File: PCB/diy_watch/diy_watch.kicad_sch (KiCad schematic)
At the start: 39 parts, among them J1 USB_B_Micro, SW1 SW_Push, U1 W25Q32JVSS, U2 DS3231MZ, U3 RP2040, U5 LTC4054ES5-4.2, U7 XC6210B332MR, Y1 12MHz_crystal

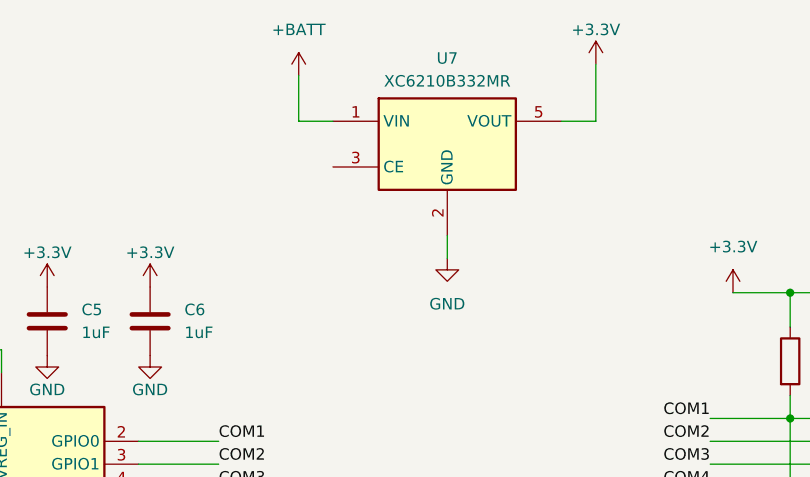
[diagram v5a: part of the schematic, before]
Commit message: Added caps to regulator, Changed edge cut
Adding missing pullup on switch
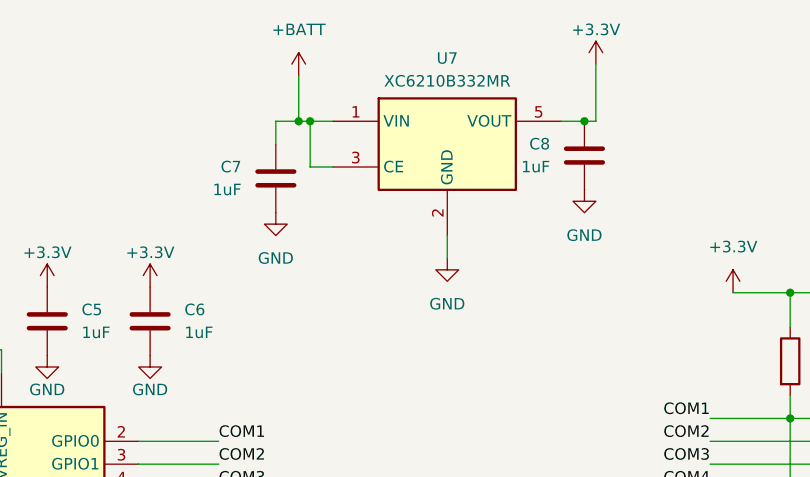
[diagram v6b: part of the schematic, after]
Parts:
- added C7, C8: 1uF, Capacitor_SMD:C_0402_1005Metric, symbol Device:C
- R11: footprint (none) -> Resistor_SMD:R_0402_1005Metric
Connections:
- net +3.3V: now also C8.1
- net +BATT: now also U7.3 (CE), C7.1
- net GND: now also C7.2, C8.2
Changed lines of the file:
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@@
   (junction (at 191.77 120.65) (diameter 0) (color 0 0 0 0)
   )
+  (junction (at 146.05 25.4) (diameter 0) (color 0 0 0 0)
+  )
   (junction (at 200.66 44.45) (diameter 0) (color 0 0 0 0)
   )
@@
   (junction (at 68.58 106.68) (diameter 0) (color 0 0 0 0)
   )
+  (junction (at 177.8 25.4) (diameter 0) (color 0 0 0 0)
+  )
   (junction (at 205.74 137.16) (diameter 0) (color 0 0 0 0)
   )
@@
   )
   (junction (at 223.52 66.04) (diameter 0) (color 0 0 0 0)
+  )
+  (junction (at 147.32 25.4) (diameter 0) (color 0 0 0 0)
   )
   (junction (at 208.28 60.96) (diameter 0) (color 0 0 0 0)
@@
     (stroke (width 0) (type default))
   )
+  (wire (pts (xy 177.8 25.4) (xy 175.26 25.4))
+    (stroke (width 0) (type default))
+  )
   (wire (pts (xy 208.28 55.88) (xy 208.28 60.96))
     (stroke (width 0) (type default))
@@
     (stroke (width 0) (type default))
   )
-  (wire (pts (xy 146.05 25.4) (xy 149.86 25.4))
+  (wire (pts (xy 146.05 25.4) (xy 147.32 25.4))
     (stroke (width 0) (type default))
   )
@@
     (stroke (width 0) (type default))
   )
+  (wire (pts (xy 147.32 25.4) (xy 149.86 25.4))
+    (stroke (width 0) (type default))
+  )
   (wire (pts (xy 215.9 55.88) (xy 215.9 63.5))
     (stroke (width 0) (type default))
@@
     (stroke (width 0) (type default))
   )
-  (wire (pts (xy 179.07 25.4) (xy 175.26 25.4))
+  (wire (pts (xy 179.07 25.4) (xy 177.8 25.4))
     (stroke (width 0) (type default))
   )
@@
     (stroke (width 0) (type default))
   )
+  (wire (pts (xy 146.05 25.4) (xy 143.51 25.4))
+    (stroke (width 0) (type default))
+  )
   (wire (pts (xy 191.77 60.96) (xy 208.28 60.96))
     (stroke (width 0) (type default))
@@
     (stroke (width 0) (type default))
   )
+  (wire (pts (xy 147.32 25.4) (xy 147.32 30.48))
+    (stroke (width 0) (type default))
+  )
   (wire (pts (xy 200.66 55.88) (xy 200.66 58.42))
     (stroke (width 0) (type default))
@@
     (stroke (width 0) (type default))
   )
+  (wire (pts (xy 147.32 30.48) (xy 149.86 30.48))
+    (stroke (width 0) (type default))
+  )
   (wire (pts (xy 215.9 63.5) (xy 246.38 63.5))
     (stroke (width 0) (type default))
@@
   )
   (wire (pts (xy 191.77 66.04) (xy 223.52 66.04))
+    (stroke (width 0) (type default))
+  )
+  (wire (pts (xy 143.51 25.4) (xy 143.51 27.94))
     (stroke (width 0) (type default))
   )
@@
       (effects (font (size 1.27 1.27)) (justify left))
     )
-    (property "Footprint" "" (at 181.102 114.3 90)
+    (property "Footprint" "Resistor_SMD:R_0402_1005Metric" (at 181.102 114.3 90)
       (effects (font (size 1.27 1.27)) hide)
     )
@@
     )
   )
+  (symbol (lib_id "power:GND") (at 177.8 33.02 0) (unit 1)
+    (in_bom yes) (on_board yes) (dnp no) (fields_autoplaced)
+    (property "Reference" "#PWR042" (at 177.8 39.37 0)
+      (effects (font (size 1.27 1.27)) hide)
+    )
+    (property "Value" "GND" (at 177.8 38.1 0)
+      (effects (font (size 1.27 1.27)))
+    )
+    (property "Footprint" "" (at 177.8 33.02 0)
+      (effects (font (size 1.27 1.27)) hide)
+    )
+    (property "Datasheet" "" (at 177.8 33.02 0)
+      (effects (font (size 1.27 1.27)) hide)
+    )
+    (pin "1")
+    (instances
+      (project "diy_watch"
+        (path "/12c7509a-2a16-4dc7-8785-00872e5a9f11"
+          (reference "#PWR042") (unit 1)
+        )
+      )
+    )
+  )
   (symbol (lib_id "power:GND") (at 162.56 40.64 0) (unit 1)
     (in_bom yes) (on_board yes) (dnp no) (fields_autoplaced)
@@
         (path "/dbb982b0-1543-45cf-9f31-f74b066d5543"
           (reference "BT1") (unit 1)
+        )
+      )
+    )
+  )
+  (symbol (lib_id "power:GND") (at 143.51 35.56 0) (unit 1)
+    (in_bom yes) (on_board yes) (dnp no) (fields_autoplaced)
+    (property "Reference" "#PWR043" (at 143.51 41.91 0)
+      (effects (font (size 1.27 1.27)) hide)
+    )
+    (property "Value" "GND" (at 143.51 40.64 0)
+      (effects (font (size 1.27 1.27)))
+    )
+    (property "Footprint" "" (at 143.51 35.56 0)
+      (effects (font (size 1.27 1.27)) hide)
+    )
+    (property "Datasheet" "" (at 143.51 35.56 0)
+      (effects (font (size 1.27 1.27)) hide)
+    )
+    (pin "1")
+    (instances
+      (project "diy_watch"
+        (path "/12c7509a-2a16-4dc7-8785-00872e5a9f11"
+          (reference "#PWR043") (unit 1)
+        )
+      )
+    )
+  )
+  (symbol (lib_id "Device:C") (at 143.51 31.75 0) (mirror y) (unit 1)
+    (in_bom yes) (on_board yes) (dnp no)
+    (property "Reference" "C7" (at 139.7 30.48 0)
+      (effects (font (size 1.27 1.27)) (justify left))
+    )
+    (property "Value" "1uF" (at 139.7 33.02 0)
+      (effects (font (size 1.27 1.27)) (justify left))
+    )
+    (property "Footprint" "Capacitor_SMD:C_0402_1005Metric" (at 142.5448 35.56 0)
+      (effects (font (size 1.27 1.27)) hide)
+    )
+    (property "Datasheet" "~" (at 143.51 31.75 0)
+      (effects (font (size 1.27 1.27)) hide)
+    )
+    (pin "1")
+    (pin "2")
+    (instances
+      (project "diy_watch"
+        (path "/12c7509a-2a16-4dc7-8785-00872e5a9f11"
+          (reference "C7") (unit 1)
         )
       )
@@
         )
       )
+    )
+  )
+  (symbol (lib_id "Device:C") (at 177.8 29.21 0) (mirror y) (unit 1)
+    (in_bom yes) (on_board yes) (dnp no)
+    (property "Reference" "C8" (at 173.99 27.94 0)
+      (effects (font (size 1.27 1.27)) (justify left))
+    )
+    (property "Value" "1uF" (at 173.99 30.48 0)
+      (effects (font (size 1.27 1.27)) (justify left))
+    )
+    (property "Footprint" "Capacitor_SMD:C_0402_1005Metric" (at 176.8348 33.02 0)
+      (effects (font (size 1.27 1.27)) hide)
+    )
+    (property "Datasheet" "~" (at 177.8 29.21 0)
+      (effects (font (size 1.27 1.27)) hide)
+    )
+    (pin "1")
+    (pin "2")
+    (instances
+      (project "diy_watch"
+        (path "/12c7509a-2a16-4dc7-8785-00872e5a9f11"
+          (reference "C8") (unit 1)
+        )
+      )

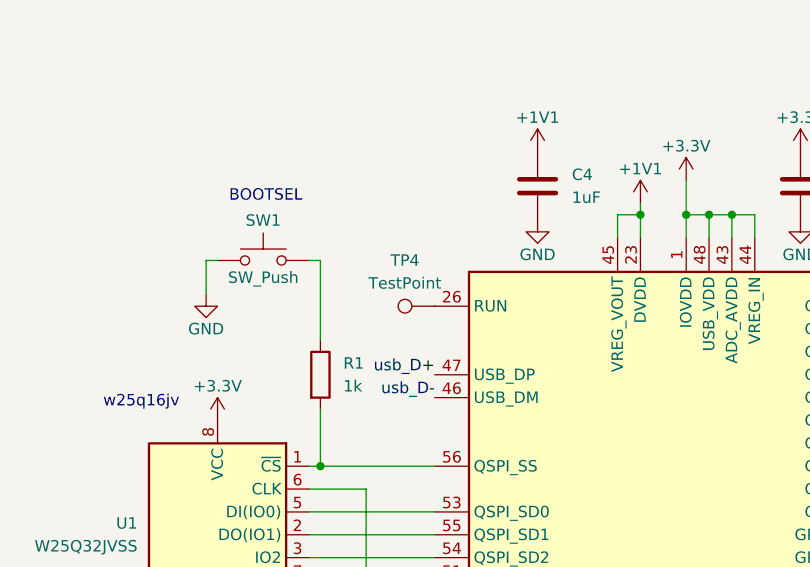
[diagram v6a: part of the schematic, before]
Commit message: Updated silkscreen names
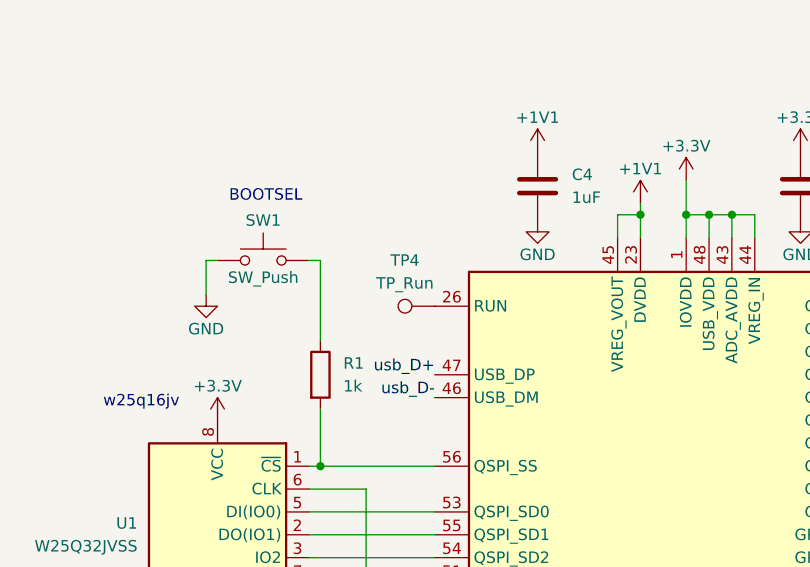
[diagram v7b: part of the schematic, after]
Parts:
- TP4: value TestPoint -> TP_Run
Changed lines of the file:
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@@
       (effects (font (size 1.27 1.27)))
     )
-    (property "Value" "TestPoint" (at 74.168 58.42 90)
+    (property "Value" "TP_Run" (at 74.168 58.42 90)
       (effects (font (size 1.27 1.27)))
     )

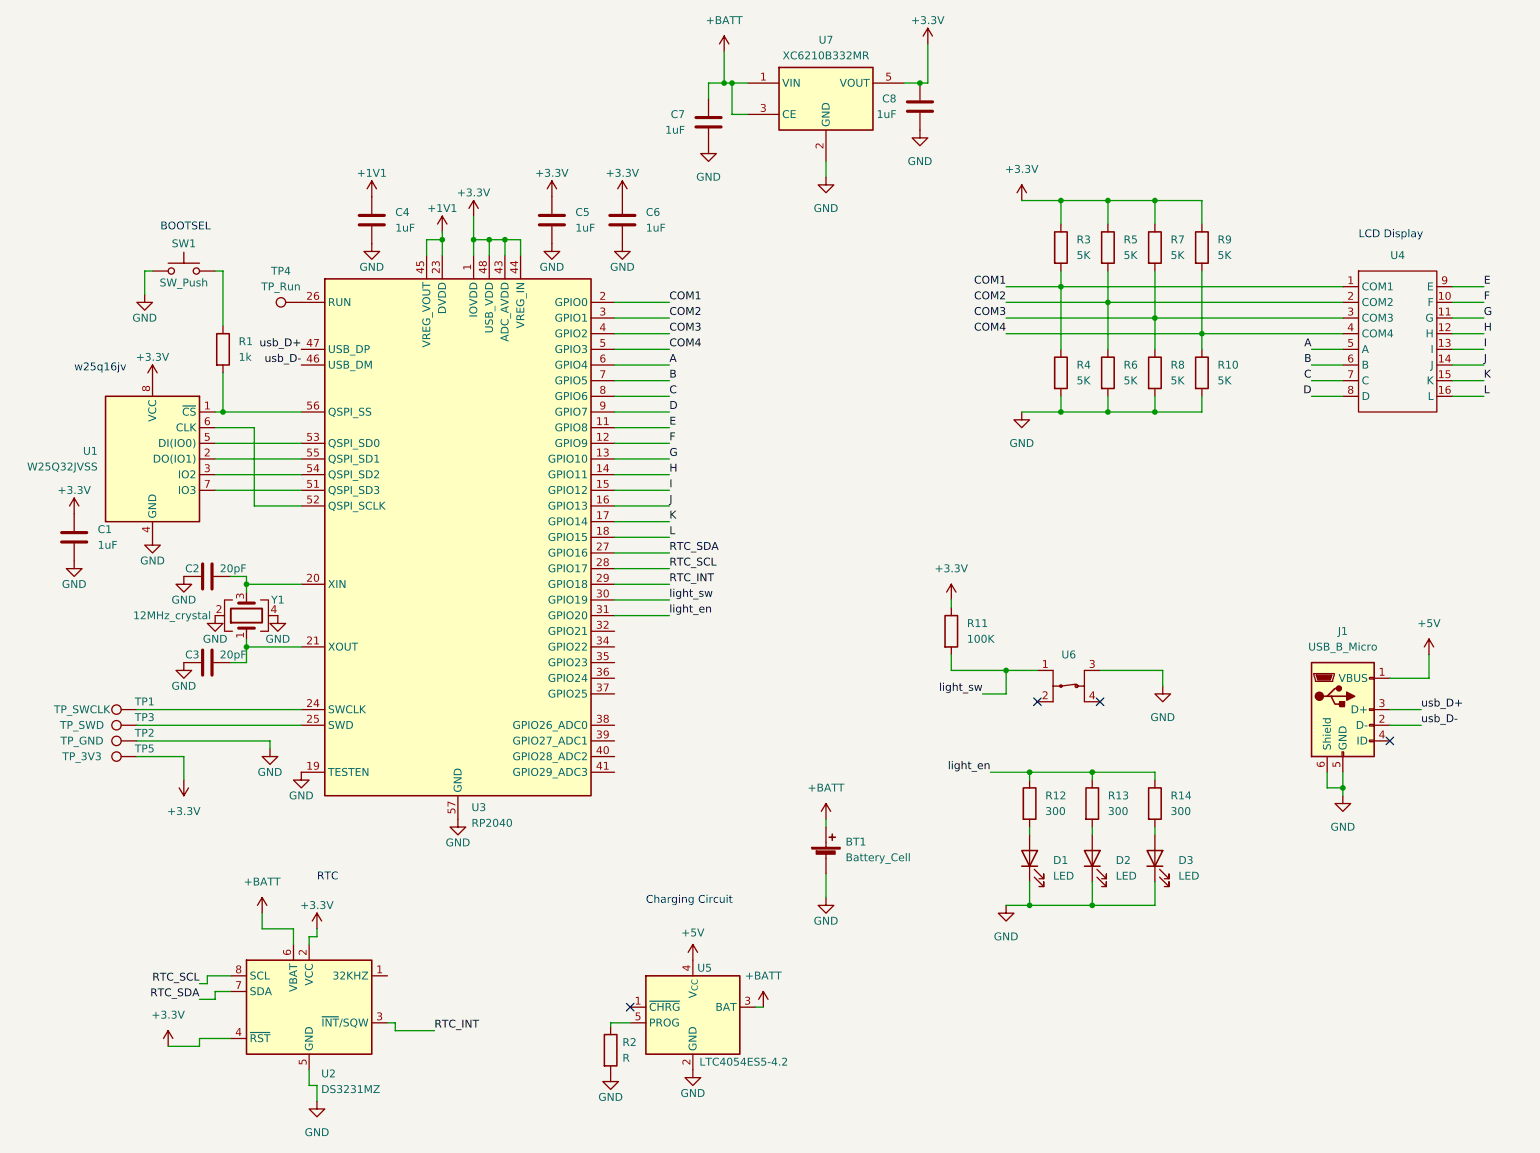
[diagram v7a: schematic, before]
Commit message: Removed wires and Rearranged PCB layout to create more space
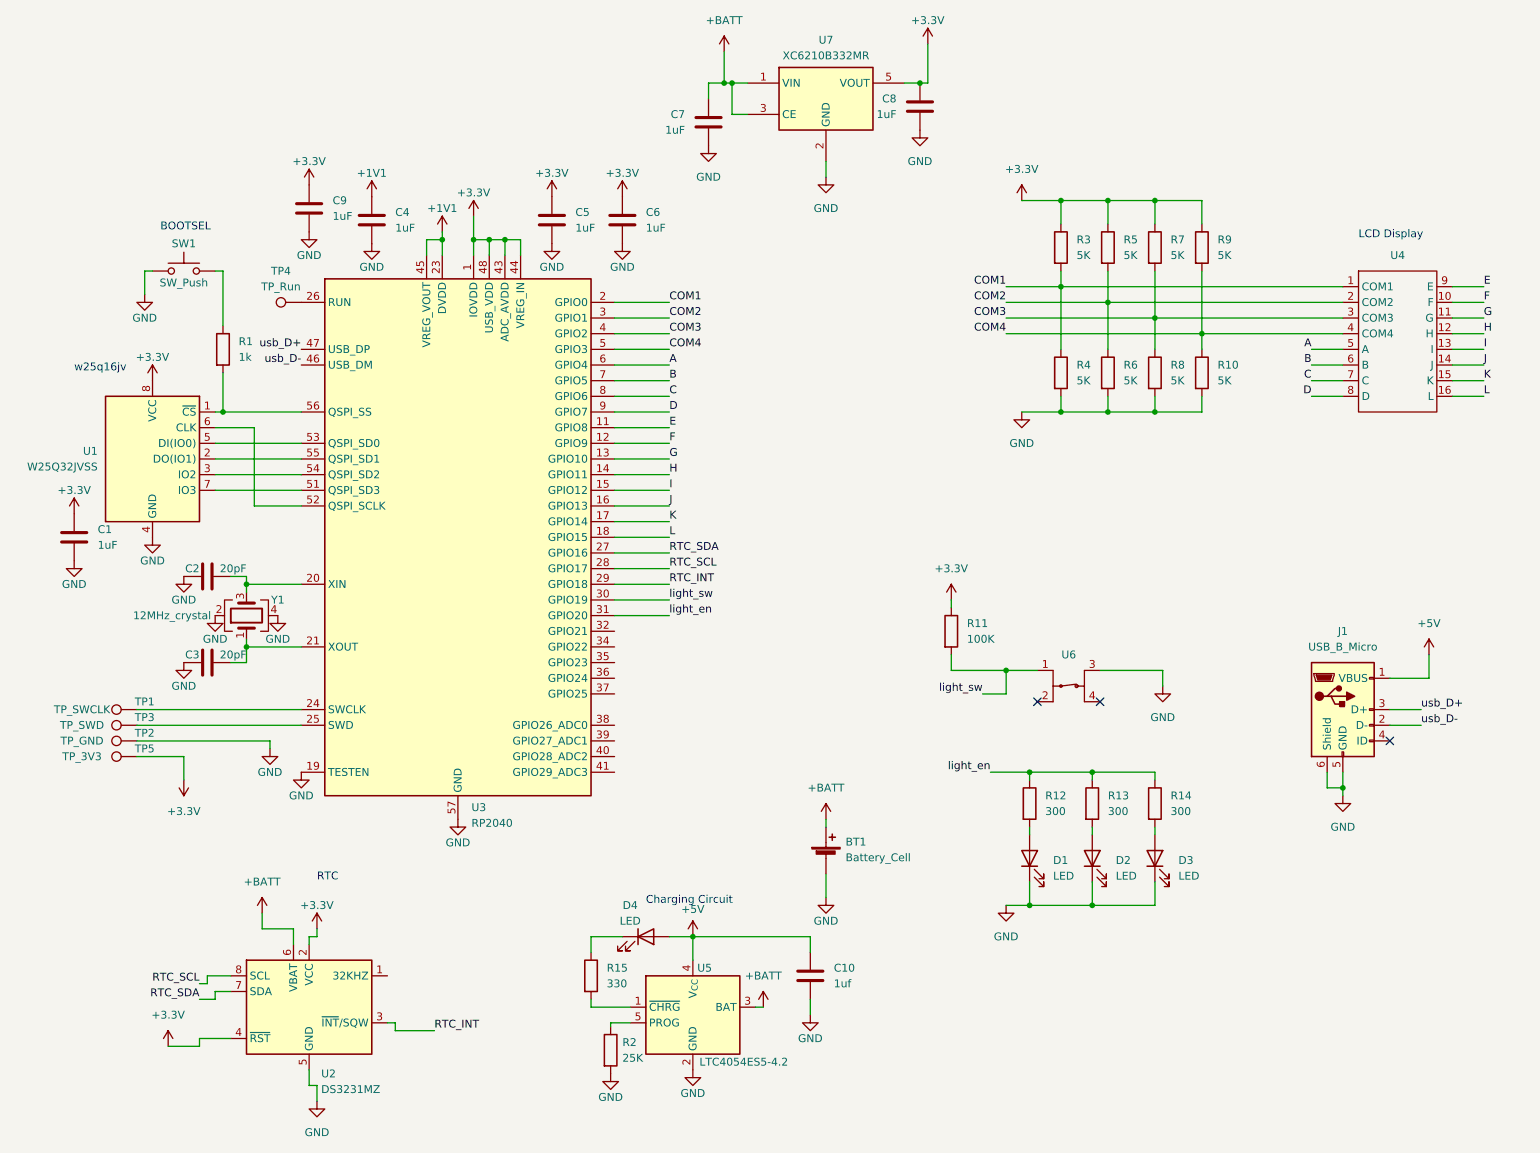
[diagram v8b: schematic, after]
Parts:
- added C10: 1uf, Capacitor_SMD:C_0402_1005Metric, symbol Device:C
- added C9: 1uF, Capacitor_SMD:C_0402_1005Metric, symbol Device:C
- added D4: LED, LED_SMD:LED_0805_2012Metric_Pad1.15x1.40mm_HandSolder, symbol Device:LED
- added R15: 330, Resistor_SMD:R_0805_2012Metric_Pad1.20x1.40mm_HandSolder, symbol Device:R
- R1: footprint Resistor_SMD:R_0603_1608Metric -> Resistor_SMD:R_0402_1005Metric
- R2: value R -> 25K
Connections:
- net +3.3V: now also C9.1
- net +5V: now also C10.1, D4.2 (A)
- net GND: now also C10.2, C9.2
- net at U5.1 (~{CHRG}): now also R15.2
- new net: D4.1 (K), R15.1
- no-connect marks 4 -> 3
